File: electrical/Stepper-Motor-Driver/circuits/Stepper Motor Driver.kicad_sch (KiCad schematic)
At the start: 30 parts, among them J1 Screw_Terminal_01x03, J2 Screw_Terminal_01x04

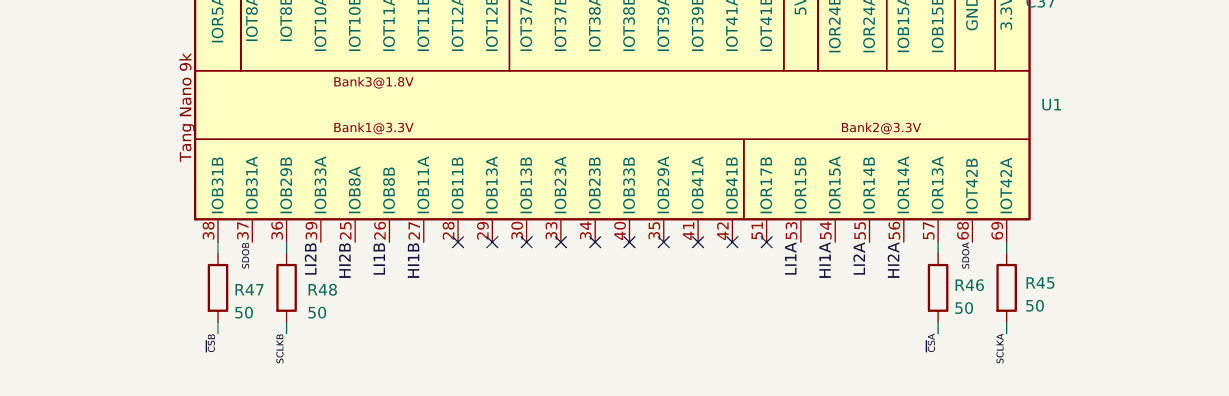
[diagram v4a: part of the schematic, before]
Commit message: Ensuring continuous ground plane below analog section
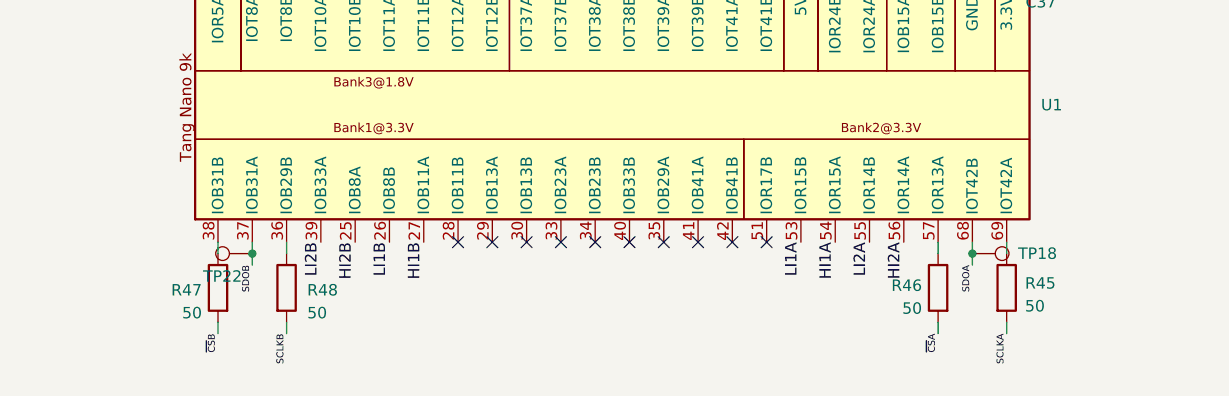
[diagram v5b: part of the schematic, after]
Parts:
- added TP18, TP22: TestPoint, Connector_PinHeader_1.00mm:PinHeader_1x01_P1.00mm_Vertical, symbol Connector:TestPoint
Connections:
- net SDOA: now also TP18.1
- net SDOB: now also TP22.1
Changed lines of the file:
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@@
 	)
 	(junction
+		(at 40.64 168.91)
+		(diameter 0)
+		(color 0 0 0 0)
+	)
+	(junction
 		(at 31.75 54.61)
 		(diameter 0)
@@
 	)
 	(junction
+		(at 120.65 168.91)
+		(diameter 0)
+		(color 0 0 0 0)
+	)
+	(junction
 		(at 92.71 54.61)
 		(diameter 0)
@@
 	(wire
 		(pts
+			(xy 120.65 170.18) (xy 120.65 168.91)
+		)
+		(stroke
+			(width 0)
+			(type default)
+		)
+	)
+	(wire
+		(pts
 			(xy 52.07 54.61) (xy 50.8 54.61)
 		)
@@
 	(wire
 		(pts
+			(xy 40.64 168.91) (xy 40.64 167.64)
+		)
+		(stroke
+			(width 0)
+			(type default)
+		)
+	)
+	(wire
+		(pts
 			(xy 74.93 45.72) (xy 74.93 39.37)
 		)
@@
 	(wire
 		(pts
+			(xy 120.65 168.91) (xy 120.65 167.64)
+		)
+		(stroke
+			(width 0)
+			(type default)
+		)
+	)
+	(wire
+		(pts
 			(xy 146.05 81.28) (xy 179.07 81.28)
 		)
@@
 	(wire
 		(pts
+			(xy 40.64 170.18) (xy 40.64 168.91)
+		)
+		(stroke
+			(width 0)
+			(type default)
+		)
+	)
+	(wire
+		(pts
 			(xy 212.09 39.37) (xy 209.55 39.37)
 		)
@@
 	)
 	(label "SDOA"
-		(at 120.65 167.64 270)
+		(at 120.65 170.18 270)
 		(effects
 			(font
@@
 	)
 	(label "SDOB"
-		(at 40.64 167.64 270)
+		(at 40.64 170.18 270)
 		(effects
 			(font
@@
 	)
 	(symbol
+		(lib_id "Connector:TestPoint")
+		(at 40.64 168.91 90)
+		(mirror x)
+		(unit 1)
+		(body_style 1)
+		(exclude_from_sim no)
+		(in_bom yes)
+		(on_board yes)
+		(in_pos_files yes)
+		(dnp no)
+		(property "Reference" "TP22"
+			(at 37.338 171.45 90)
+			(show_name no)
+			(do_not_autoplace no)
+			(effects
+				(font
+					(size 1.27 1.27)
+				)
+			)
+		)
+		(property "Value" "TestPoint"
+			(at 38.6079 171.45 0)
+			(hide yes)
+			(show_name no)
+			(do_not_autoplace no)
+			(effects
+				(font
+					(size 1.27 1.27)
+				)
+				(justify left)
+			)
+		)
+		(property "Footprint" "Connector_PinHeader_1.00mm:PinHeader_1x01_P1.00mm_Vertical"
+			(at 40.64 173.99 0)
+			(hide yes)
+			(show_name no)
+			(do_not_autoplace no)
+			(effects
+				(font
+					(size 1.27 1.27)
+				)
+			)
+		)
+		(property "Datasheet" ""
+			(at 40.64 173.99 0)
+			(hide yes)
+			(show_name no)
+			(do_not_autoplace no)
+			(effects
+				(font
+					(size 1.27 1.27)
+				)
+			)
+		)
+		(property "Description" "test point"
+			(at 40.64 168.91 0)
+			(hide yes)
+			(show_name no)
+			(do_not_autoplace no)
+			(effects
+				(font
+					(size 1.27 1.27)
+				)
+			)
+		)
+		(pin "1"
+		)
+		(instances
+			(project "Stepper Motor Driver"
+				(path "/c25060f1-f2f3-4cbd-b6ee-5f66e19502f5"
+					(reference "TP22")
+					(unit 1)
+				)
+			)
+		)
+	)
+	(symbol
 		(lib_id "power:GND")
 		(at 132.08 133.35 90)
@@
 		(lib_id "Device:R")
 		(at 116.84 172.72 0)
+		(mirror y)
 		(unit 1)
 		(body_style 1)
@@
 		(dnp no)
 		(property "Reference" "R46"
-			(at 118.618 172.466 0)
+			(at 115.062 172.466 0)
 			(show_name no)
 			(do_not_autoplace no)
@@
 		)
 		(property "Value" "50"
-			(at 118.618 175.006 0)
+			(at 115.062 175.006 0)
 			(show_name no)
 			(do_not_autoplace no)
@@
 		)
 		(property "Footprint" "Resistor_SMD:R_1206_3216Metric"
-			(at 115.062 172.72 90)
+			(at 118.618 172.72 90)
 			(hide yes)
 			(show_name no)
@@
 		(lib_id "Device:R")
 		(at 36.83 172.72 0)
+		(mirror y)
 		(unit 1)
 		(body_style 1)
@@
 		(dnp no)
 		(property "Reference" "R47"
-			(at 38.608 172.974 0)
+			(at 35.052 172.974 0)
 			(show_name no)
 			(do_not_autoplace no)
@@
 		)
 		(property "Value" "50"
-			(at 38.608 175.514 0)
+			(at 35.052 175.514 0)
 			(show_name no)
 			(do_not_autoplace no)
@@
 		)
 		(property "Footprint" "Resistor_SMD:R_1206_3216Metric"
-			(at 35.052 172.72 90)
+			(at 38.608 172.72 90)
 			(hide yes)
 			(show_name no)
@@
 					(unit 1)
 				)
+			)
+		)
+	)
+	(symbol
+		(lib_id "Connector:TestPoint")
+		(at 120.65 168.91 270)
+		(unit 1)
+		(body_style 1)
+		(exclude_from_sim no)
+		(in_bom yes)
+		(on_board yes)
+		(in_pos_files yes)
+		(dnp no)
+		(fields_autoplaced yes)
+		(property "Reference" "TP18"
+			(at 125.73 168.9099 90)
+			(show_name no)
+			(do_not_autoplace no)
+			(effects
+				(font
+					(size 1.27 1.27)
+				)
+				(justify left)
+			)
+		)
+		(property "Value" "TestPoint"
+			(at 122.6821 171.45 0)
+			(hide yes)
+			(show_name no)
+			(do_not_autoplace no)
+			(effects
+				(font
+					(size 1.27 1.27)
+				)
+				(justify left)
+			)
+		)
+		(property "Footprint" "Connector_PinHeader_1.00mm:PinHeader_1x01_P1.00mm_Vertical"
+			(at 120.65 173.99 0)
+			(hide yes)
+			(show_name no)
+			(do_not_autoplace no)
+			(effects
+				(font
+					(size 1.27 1.27)
+				)
+			)
+		)
+		(property "Datasheet" ""
+			(at 120.65 173.99 0)
+			(hide yes)
+			(show_name no)
+			(do_not_autoplace no)
+			(effects
+				(font
+					(size 1.27 1.27)
+				)
+			)
+		)
+		(property "Description" "test point"
+			(at 120.65 168.91 0)
+			(hide yes)
+			(show_name no)
+			(do_not_autoplace no)
+			(effects
+				(font
+					(size 1.27 1.27)
+				)
+			)
+		)
+		(pin "1"
+		)
+		(instances
+			(project "Stepper Motor Driver"
+				(path "/c25060f1-f2f3-4cbd-b6ee-5f66e19502f5"
+					(reference "TP18")
+					(unit 1)
+				)

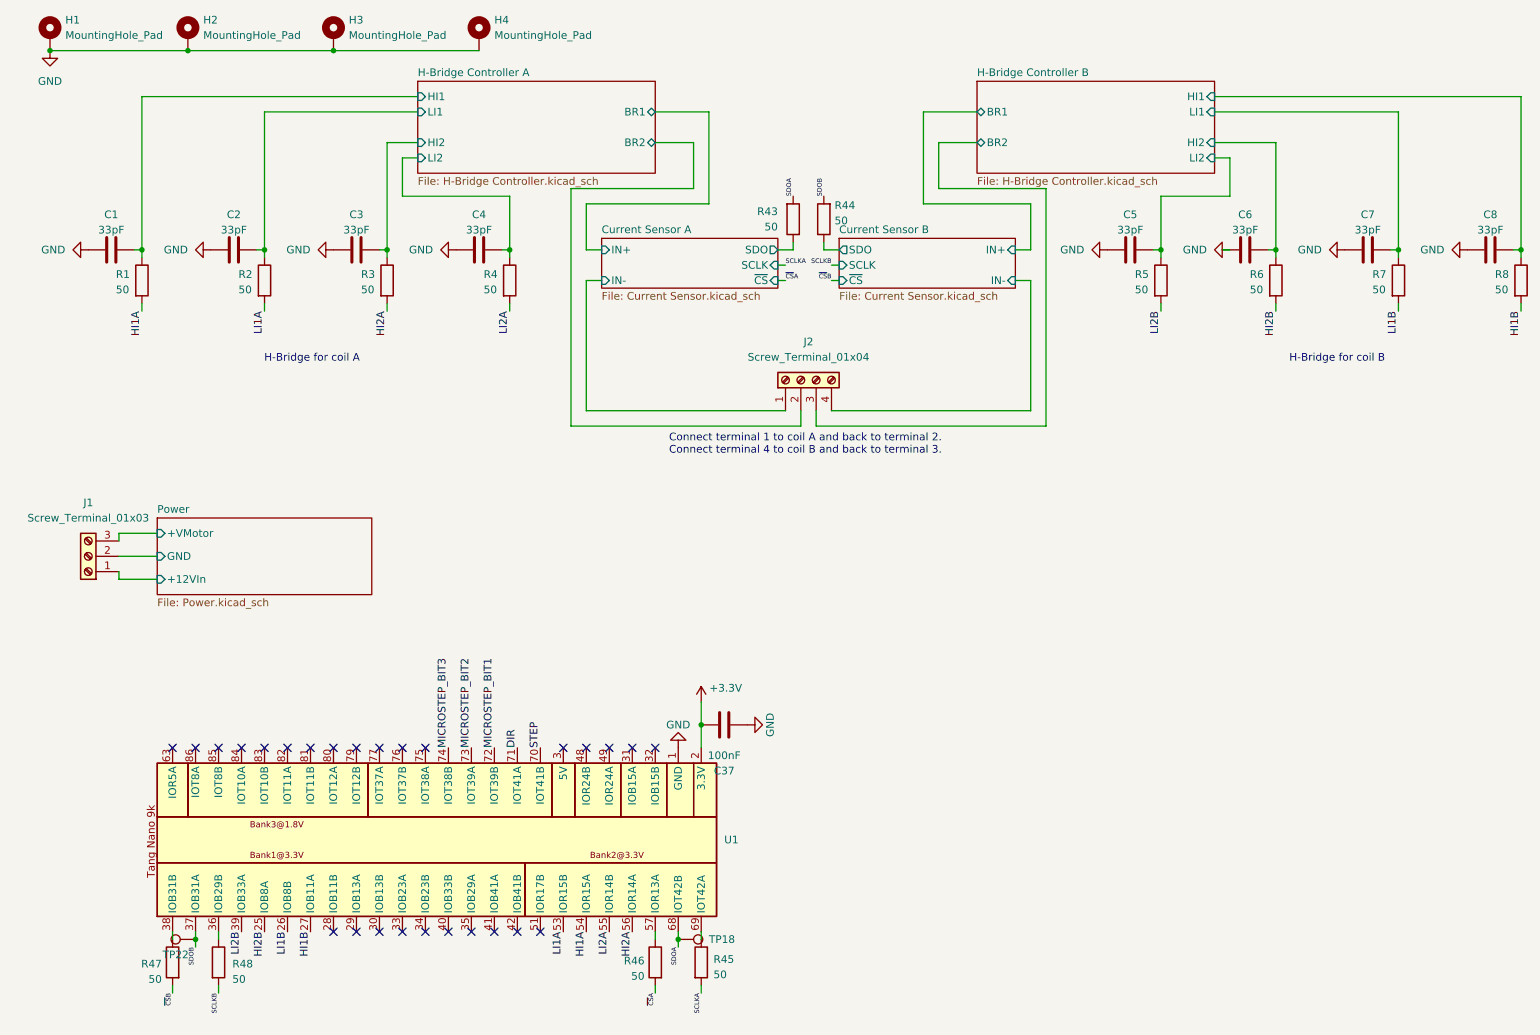
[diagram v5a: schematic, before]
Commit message: Compressing layout to 100mm x 100mm
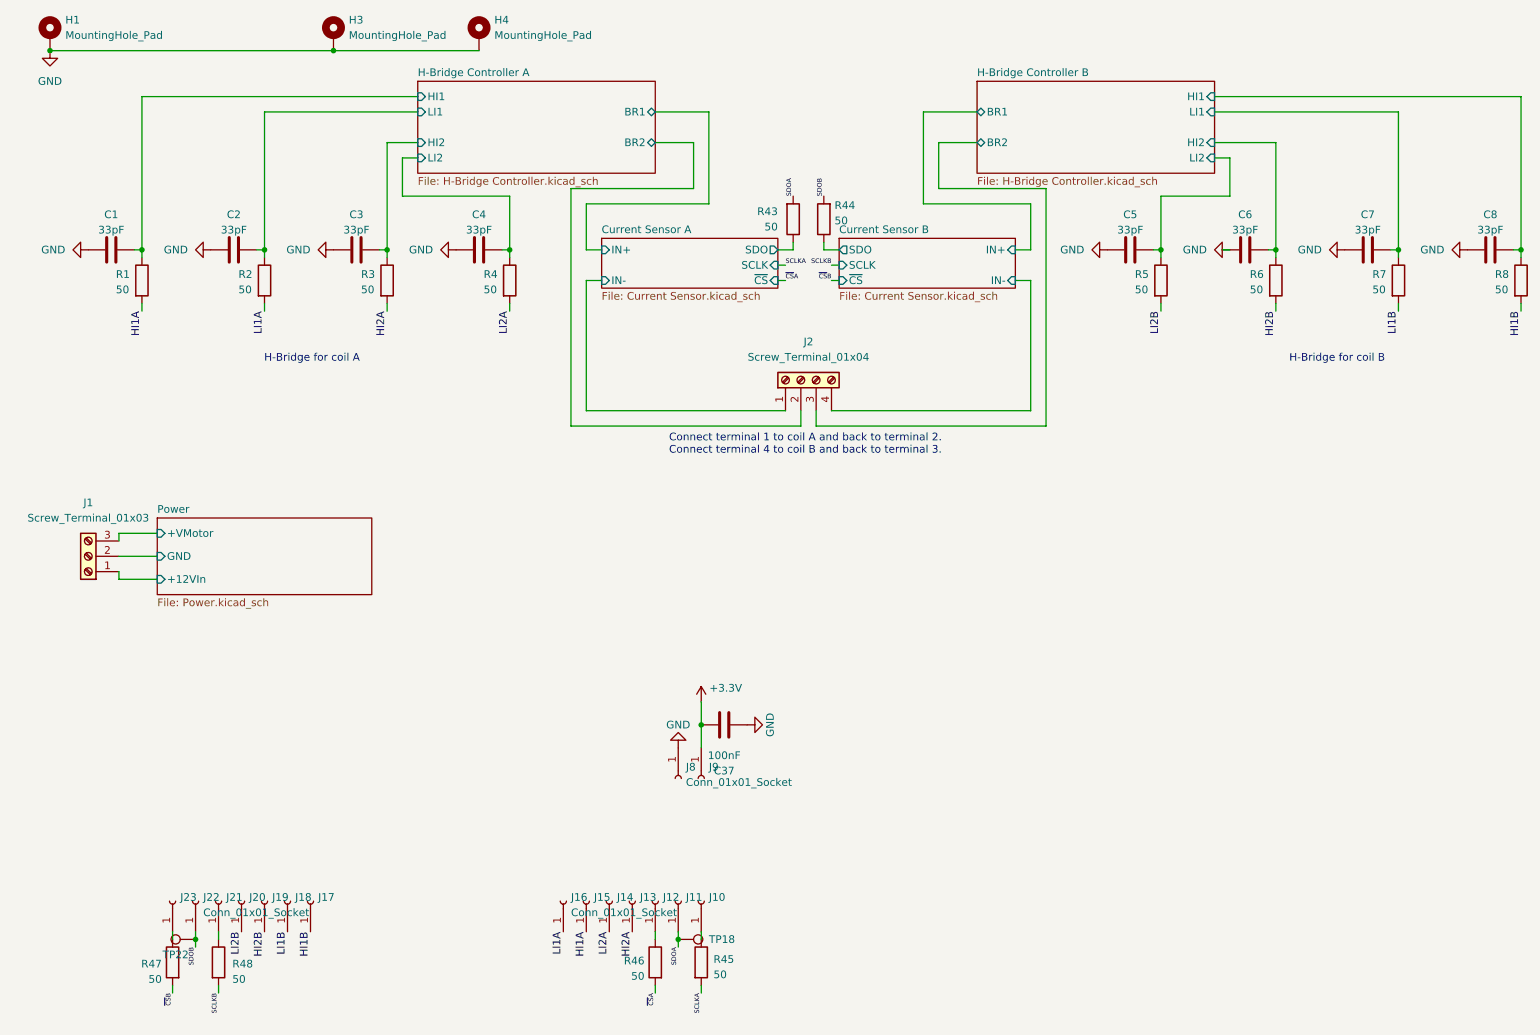
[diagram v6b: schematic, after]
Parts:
- removed H2: MountingHole_Pad, MountingHole:MountingHole_2.2mm_M2_DIN965_Pad, symbol Mechanical:MountingHole_Pad
- removed U1: (no value), Tang Nano 9k:Tang Nano 9k Header Pins, symbol Tang Nano 9k:Tang_Nano_9k
- added J10, J11, J12, J13, J14, J15, J16, J17, J18, J19, J20, J21, J22, J23, J8, J9: Conn_01x01_Socket, TestPoint:TestPoint_Pad_D2.0mm, symbol Connector:Conn_01x01_Socket
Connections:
- net +3.3V: now also J9.1 (Pin_1)
- net GND: now also J8.1 (Pin_1)
- net HI1A: now also J15.1 (Pin_1)
- net HI1B: now also J17.1 (Pin_1)
- net HI2A: now also J13.1 (Pin_1)
- net HI2B: now also J19.1 (Pin_1)
- net LI1A: now also J16.1 (Pin_1)
- net LI1B: now also J18.1 (Pin_1)
- net LI2A: now also J14.1 (Pin_1)
- net LI2B: now also J20.1 (Pin_1)
- net SDOA: now also J11.1 (Pin_1)
- net SDOB: now also J22.1 (Pin_1)
- net at R45.1: now also J10.1 (Pin_1)
- net at R46.1: now also J12.1 (Pin_1)
- net at R48.1: now also J21.1 (Pin_1)
- net at R47.1: now also J23.1 (Pin_1)
- no-connect marks 27 -> 0

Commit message: Adding fiducial marks
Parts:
- added FID1, FID2: Fiducial, Fiducial:Fiducial_1mm_Mask3mm, symbol Mechanical:Fiducial
- J10, J11, J12, J13, J14, J15, J16, J17, J18, J19, J20, J21, J22, J23, J8, J9: now left out of the parts list
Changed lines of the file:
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@@
 		(body_style 1)
 		(exclude_from_sim no)
-		(in_bom yes)
+		(in_bom no)
 		(on_board yes)
 		(in_pos_files yes)
@@
 		(body_style 1)
 		(exclude_from_sim no)
-		(in_bom yes)
+		(in_bom no)
 		(on_board yes)
 		(in_pos_files yes)
@@
 		(body_style 1)
 		(exclude_from_sim no)
-		(in_bom yes)
+		(in_bom no)
 		(on_board yes)
 		(in_pos_files yes)
@@
 		(body_style 1)
 		(exclude_from_sim no)
-		(in_bom yes)
+		(in_bom no)
 		(on_board yes)
 		(in_pos_files yes)
@@
 	)
 	(symbol
+		(lib_id "Mechanical:Fiducial")
+		(at 118.11 17.78 0)
+		(unit 1)
+		(body_style 1)
+		(exclude_from_sim no)
+		(in_bom no)
+		(on_board yes)
+		(in_pos_files yes)
+		(dnp no)
+		(fields_autoplaced yes)
+		(property "Reference" "FID1"
+			(at 120.65 16.5099 0)
+			(show_name no)
+			(do_not_autoplace no)
+			(effects
+				(font
+					(size 1.27 1.27)
+				)
+				(justify left)
+			)
+		)
+		(property "Value" "Fiducial"
+			(at 120.65 19.0499 0)
+			(show_name no)
+			(do_not_autoplace no)
+			(effects
+				(font
+					(size 1.27 1.27)
+				)
+				(justify left)
+			)
+		)
+		(property "Footprint" "Fiducial:Fiducial_1mm_Mask3mm"
+			(at 118.11 17.78 0)
+			(hide yes)
+			(show_name no)
+			(do_not_autoplace no)
+			(effects
+				(font
+					(size 1.27 1.27)
+				)
+			)
+		)
+		(property "Datasheet" ""
+			(at 118.11 17.78 0)
+			(hide yes)
+			(show_name no)
+			(do_not_autoplace no)
+			(effects
+				(font
+					(size 1.27 1.27)
+				)
+			)
+		)
+		(property "Description" "Fiducial Marker"
+			(at 118.11 17.78 0)
+			(hide yes)
+			(show_name no)
+			(do_not_autoplace no)
+			(effects
+				(font
+					(size 1.27 1.27)
+				)
+			)
+		)
+		(instances
+			(project "Stepper Motor Driver"
+				(path "/c25060f1-f2f3-4cbd-b6ee-5f66e19502f5"
+					(reference "FID1")
+					(unit 1)
+				)
+			)
+		)
+	)
+	(symbol
 		(lib_id "Connector:Conn_01x01_Socket")
 		(at 120.65 162.56 90)
@@
 		(body_style 1)
 		(exclude_from_sim no)
-		(in_bom yes)
+		(in_bom no)
 		(on_board yes)
 		(in_pos_files yes)
@@
 		(body_style 1)
 		(exclude_from_sim no)
-		(in_bom yes)
+		(in_bom no)
 		(on_board yes)
 		(in_pos_files yes)
@@
 		(body_style 1)
 		(exclude_from_sim no)
-		(in_bom yes)
+		(in_bom no)
 		(on_board yes)
 		(in_pos_files yes)
@@
 		(body_style 1)
 		(exclude_from_sim no)
-		(in_bom yes)
+		(in_bom no)
 		(on_board yes)
 		(in_pos_files yes)
@@
 	)
 	(symbol
+		(lib_id "Mechanical:Fiducial")
+		(at 133.35 17.78 0)
+		(unit 1)
+		(body_style 1)
+		(exclude_from_sim no)
+		(in_bom no)
+		(on_board yes)
+		(in_pos_files yes)
+		(dnp no)
+		(fields_autoplaced yes)
+		(property "Reference" "FID2"
+			(at 135.89 16.5099 0)
+			(show_name no)
+			(do_not_autoplace no)
+			(effects
+				(font
+					(size 1.27 1.27)
+				)
+				(justify left)
+			)
+		)
+		(property "Value" "Fiducial"
+			(at 135.89 19.0499 0)
+			(show_name no)
+			(do_not_autoplace no)
+			(effects
+				(font
+					(size 1.27 1.27)
+				)
+				(justify left)
+			)
+		)
+		(property "Footprint" "Fiducial:Fiducial_1mm_Mask3mm"
+			(at 133.35 17.78 0)
+			(hide yes)
+			(show_name no)
+			(do_not_autoplace no)
+			(effects
+				(font
+					(size 1.27 1.27)
+				)
+			)
+		)
+		(property "Datasheet" ""
+			(at 133.35 17.78 0)
+			(hide yes)
+			(show_name no)
+			(do_not_autoplace no)
+			(effects
+				(font
+					(size 1.27 1.27)
+				)
+			)
+		)
+		(property "Description" "Fiducial Marker"
+			(at 133.35 17.78 0)
+			(hide yes)
+			(show_name no)
+			(do_not_autoplace no)
+			(effects
+				(font
+					(size 1.27 1.27)
+				)
+			)
+		)
+		(instances
+			(project "Stepper Motor Driver"
+				(path "/c25060f1-f2f3-4cbd-b6ee-5f66e19502f5"
+					(reference "FID2")
+					(unit 1)
+				)
+			)
+		)
+	)
+	(symbol
 		(lib_id "Connector:Conn_01x01_Socket")
 		(at 55.88 162.56 90)
@@
 		(body_style 1)
 		(exclude_from_sim no)
-		(in_bom yes)
+		(in_bom no)
 		(on_board yes)
 		(in_pos_files yes)
@@
 		(body_style 1)
 		(exclude_from_sim no)
-		(in_bom yes)
+		(in_bom no)
 		(on_board yes)
 		(in_pos_files yes)
@@
 		(body_style 1)
 		(exclude_from_sim no)
-		(in_bom yes)
+		(in_bom no)
 		(on_board yes)
 		(in_pos_files yes)
@@
 		(body_style 1)
 		(exclude_from_sim no)
-		(in_bom yes)
+		(in_bom no)
 		(on_board yes)
 		(in_pos_files yes)
@@
 		(body_style 1)
 		(exclude_from_sim no)
-		(in_bom yes)
+		(in_bom no)
 		(on_board yes)
 		(in_pos_files yes)
@@
 		(body_style 1)
 		(exclude_from_sim no)
-		(in_bom yes)
+		(in_bom no)
 		(on_board yes)
 		(in_pos_files yes)
@@
 		(body_style 1)
 		(exclude_from_sim no)
-		(in_bom yes)
+		(in_bom no)
 		(on_board yes)
 		(in_pos_files yes)
@@
 		(body_style 1)
 		(exclude_from_sim no)
-		(in_bom yes)
+		(in_bom no)
 		(on_board yes)
 		(in_pos_files yes)
